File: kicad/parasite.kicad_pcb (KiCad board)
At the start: 2 copper layers, 22 x 126.4 mm, 33 parts, among them Q1 MMBT3904, Q2 MMBT3904, Q3 AO3407, Q4 Q_Photo_NPN, U1 E73-2G4M08S1C-52840, U2 SHTC3, Y1 32.768kHz

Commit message: Initial routing complete
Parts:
- removed C6: 100p, Capacitor_SMD:C_0402_1005Metric
- removed Cpara1: 5p, Capacitor_SMD:C_0805_2012Metric
- removed PHT: PHOTO_OUT, TestPoint:TestPoint_Pad_D1.0mm
- removed Q2: MMBT3904, Package_TO_SOT_SMD:SOT-23
- removed Q3: AO3407, Package_TO_SOT_SMD:SOT-23
- removed R3, R5: 1k, Resistor_SMD:R_0402_1005Metric
- added S1: B3U-1000P, snapeda:SW_B3U-1000P, F.Cu at (72.3, 50.2)
- added S2: B3U-1000P, snapeda:SW_B3U-1000P, F.Cu at (68.5, 50.2)
- added TP3: GND, TestPoint:TestPoint_Pad_D1.0mm, F.Cu at (77.4, 39.8)
- Q1: value MMBT3904 -> 2N3906
- TP4: value VSO -> RST
- TP5: value RST -> CPARA
- TP6: value GND -> PWM
- U1: value E73-2G4M08S1C-52840 -> E73-2G4M08S1C; footprint nrfmicro:E73-2G4M08S1C-52840 -> snapeda:E73-2G4M08S1C-modified
- moved TP6 23.2 mm to (61.4, 59.5), turned to 180 degrees
- moved TP5 16.7 mm to (68.0, 58.8), turned to 180 degrees
- moved TP4 10.6 mm to (77.4, 42.3), turned to -90 degrees
- moved U1 8.63 mm to (67.0, 36.6), turned to 0 degrees
- moved R6 8.46 mm to (71.5, 59.1), turned to -90 degrees
- moved C1 8.34 mm to (69.8, 59.1), turned to -90 degrees
- moved R8 6.44 mm to (76.2, 53.0), turned to 90 degrees
- moved R7 6.28 mm to (74.6, 53.0), turned to -90 degrees
- moved U2 5.59 mm to (74.1, 56.0)
- moved Q4 3.09 mm to (58.1, 32.7), turned to 90 degrees
- moved C2 2.81 mm to (70.5, 55.4), turned to 90 degrees
- moved R2 2.76 mm to (61.5, 50.2), turned to 180 degrees
- moved TP1 2.30 mm to (77.4, 34.7), turned to -90 degrees
- moved TP2 2.30 mm to (77.4, 37.2), turned to -90 degrees
- moved TP7 2.30 mm to (77.4, 32.2), turned to -90 degrees
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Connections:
- net /PHOTO_OUT renamed PHOTO_OUT
- net /PHOTO_V renamed PHOTO_V
- net /SCL renamed SCL
- net /SDA renamed SDA
- net Net-(TP1-Pad1) renamed SWDIO
- net Net-(TP2-Pad1) renamed SWDCLK
- BT1 pad 1: Net-(BT1-Pad1) -> +3V0
- C1 pad 1: /SENS_OUT -> SENS_OUT
- C3 pad 1: Net-(C3-Pad1) -> GND
- C3 pad 2: GND -> Net-(C3-Pad2)
- C4 pad 1: GND -> Net-(C4-Pad1)
- C4 pad 2: Net-(C4-Pad2) -> GND
- D1 pad 1: /SENS_OUT -> SENS_OUT
- D1 pad 2: /Csen+ -> CPARA
- Q1 pad 1: Net-(C6-Pad1) -> CPARA
- Q1 pad 2: GND -> Net-(R4-Pad1)
- Q1 pad 3: Net-(Q1-Pad3) -> GND
- R1 pad 1: /PWM -> PWM
- R1 pad 2: /Csen+ -> CPARA
- R2 pad 1: /LED -> Net-(D2-Pad2)
- R2 pad 2: Net-(D2-Pad2) -> LED
- R4 pad 1: Net-(C6-Pad1) -> Net-(R4-Pad1)
- R4 pad 2: /PWM -> PWM
- R6 pad 1: /SENS_OUT -> SENS_OUT
- TP4 pad 1: /SENS_OUT -> RST
- TP5 pad 1: Net-(TP5-Pad1) -> CPARA
- TP6 pad 1: GND -> PWM
- U1 pad 1: Net-(U1-Pad1) -> unconnected-(U1-Pad1)
- U1 pad 10: Net-(U1-Pad10) -> unconnected-(U1-Pad10)
- U1 pad 11: Net-(C3-Pad1) -> Net-(C3-Pad2)
- U1 pad 13: Net-(C4-Pad2) -> Net-(C4-Pad1)
- U1 pad 15: /PWM -> PWM
- U1 pad 17: Net-(U1-Pad17) -> BTN1
- U1 pad 2: /FAST_DISCH_EN -> unconnected-(U1-Pad2)
- U1 pad 25: Net-(U1-Pad25) -> unconnected-(U1-Pad25)
- U1 pad 26: Net-(TP5-Pad1) -> RST
- U1 pad 27: Net-(U1-Pad27) -> unconnected-(U1-Pad27)
- U1 pad 29: Net-(U1-Pad29) -> unconnected-(U1-Pad29)
- U1 pad 3: /SENS_OUT -> SENS_OUT
- U1 pad 31: Net-(U1-Pad31) -> unconnected-(U1-Pad31)
- U1 pad 4: /LED -> LED
- U1 pad 41: Net-(U1-Pad41) -> unconnected-(U1-Pad41)
- U1 pad 43: Net-(U1-Pad43) -> unconnected-(U1-Pad43)
- U1 pad 6: Net-(U1-Pad6) -> unconnected-(U1-Pad6)
- U1 pad 9: Net-(U1-Pad9) -> unconnected-(U1-Pad9)
- U2 pad 5: Net-(U2-Pad5) -> unconnected-(U2-Pad5)
- Y1 pad 1: Net-(C3-Pad1) -> Net-(C4-Pad1)
- Y1 pad 2: Net-(C4-Pad2) -> Net-(C3-Pad2)
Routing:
- net /Csen+: track 104.6 -> 0.00 mm
- net CPARA: track 0.00 -> 91.2 mm
- net /SENS_OUT: track 78.6 -> 0.00 mm, vias 3 -> 0
- net Net-(BT1-Pad1): track 47.6 -> 0.00 mm, vias 3 -> 0
- net /FAST_DISCH_EN: track 40.9 -> 0.00 mm, vias 2 -> 0
- net SENS_OUT: track 0.00 -> 37.6 mm, vias 0 -> 2
- net +3V0: track 37.8 -> 72.3 mm, vias 0 -> 6
- net /PWM: track 19.4 -> 0.00 mm
- net PWM: track 0.00 -> 19.4 mm, vias 0 -> 2
- net LED: track 0.00 -> 16.8 mm, vias 0 -> 2
- net /LED: track 14.2 -> 0.00 mm, vias 2 -> 0
- net RST: track 0.00 -> 11.9 mm, vias 0 -> 2
- net Net-(C4-Pad2): track 8.33 -> 0.00 mm
- net SWDCLK: track 14.5 -> 6.42 mm, vias 3 -> 2
- net Net-(C4-Pad1): track 0.00 -> 7.96 mm
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
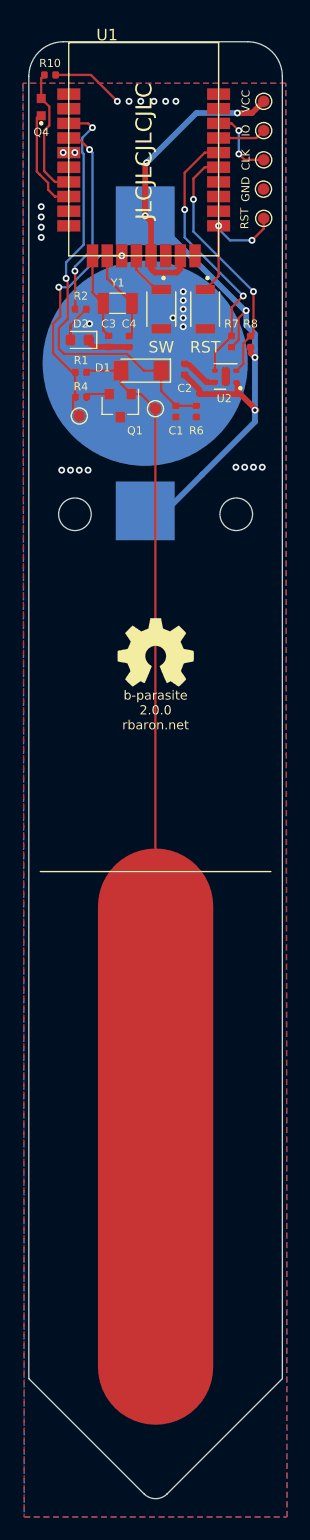
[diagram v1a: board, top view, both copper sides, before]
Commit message: Adds sketch of RC circuit in silkscreen
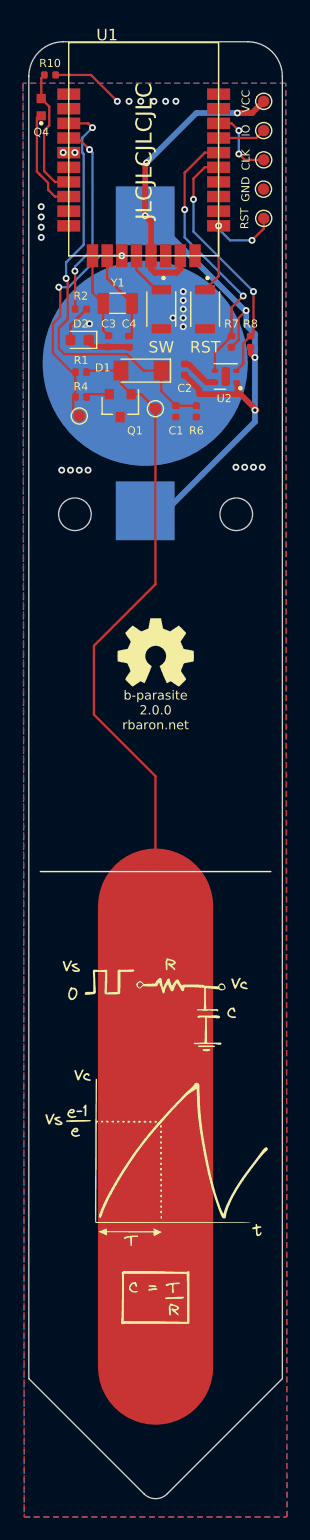
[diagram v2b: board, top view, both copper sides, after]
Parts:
- added G***: LOGO, drawing:circuit_drawing, F.Cu at (68.0, 122.2)
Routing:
- net CPARA: track 91.2 -> 95.6 mm

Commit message: Slightly better routing
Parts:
- U1: footprint snapeda:E73-2G4M08S1C-modified -> snapeda:E73-2G4M08S1C
- moved BT1 0.26 mm to (67.1, 55.2)
- renumbered S1 to RST, S2 to SW1
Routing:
- net +3V0: track 72.3 -> 76.5 mm, vias 6 -> 8
- net GND: track 13.1 -> 16.8 mm, vias 27 -> 29
- net SDA: track 24.0 -> 24.5 mm
